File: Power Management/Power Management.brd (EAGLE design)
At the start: 22.2 x 10.2 mm, 7 parts, among them IC1 BH67172NUX, IC2 BH67172NUX, X1 52745-0690, X2 52745-0690

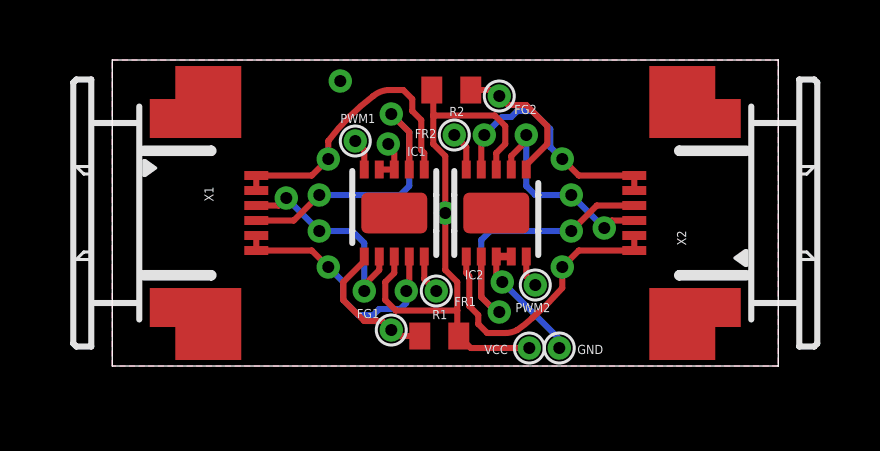
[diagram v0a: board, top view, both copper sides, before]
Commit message: Added Power Management reference design
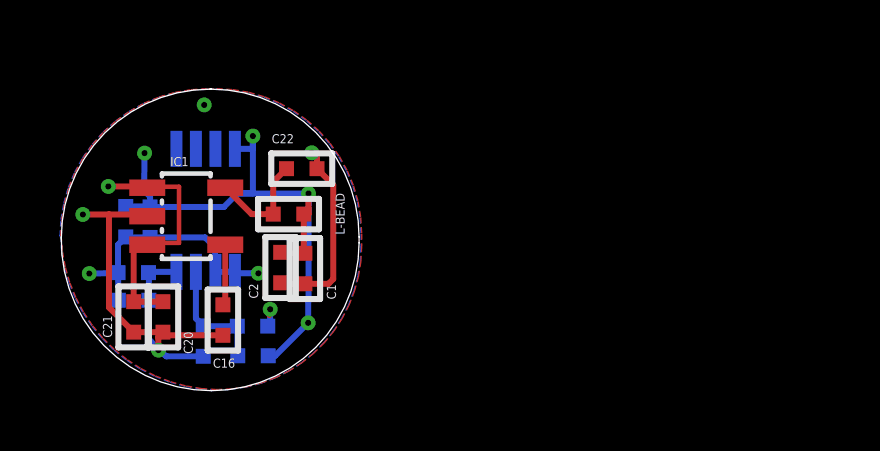
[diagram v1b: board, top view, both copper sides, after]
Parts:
- removed X1, X2: 52745-0690, con-molex:52745-0690
- added C1, C10, C11, C21: 10u, rc-master-smd:C0402
- added C16, C23: 10n, rc-master-smd:C0402
- added C2, C20, C22, C4, C5: 100n, rc-master-smd:C0402
- added L-BEAD: (no value), L-Bead:0402
- IC1: value BH67172NUX -> TPS732XX; device rohm:VSON010X3030 -> TPS732xx:SOT23
- IC2: value BH67172NUX -> AD8617; device rohm:VSON010X3030 -> ad8617:MSOP8
- R1, R2: value 10k -> (none); device resistor:R0402 -> rc-master-smd:R0402
- moved GOLD_ORB_SM1 16.0 mm to (12.6, 2.20)
- moved R2 10.3 mm to (7.28, 2.83), flipped to the bottom, turned to 0 degrees
- moved IC2 9.69 mm to (5.71, 6.69), flipped to the bottom, turned to 0 degrees
- moved IC1 6.94 mm to (5.07, 6.49), turned to 270 degrees
- moved R1 6.25 mm to (7.29, 1.84), flipped to the bottom, turned to 180 degrees
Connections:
- removed net +3V3: IC1.3, IC2.3, R1.2, R2.2
- removed net COM1: IC1.2, X1.3
- removed net COM2: IC2.2, X2.3
- removed net FG1: IC1.1, R1.1
- removed net FG2: IC2.1, R2.1
- removed net FR1: IC1.5
- removed net FR2: IC2.5
- removed net GND: IC1.8, IC1.9, IC2.8, IC2.9
- removed net PWM1: IC1.10
- removed net PWM2: IC2.10
- removed net U1: IC1.4, X1.5, X1.6
- removed net U2: IC2.4, X2.5, X2.6
- removed net V1: IC1.7, X1.4
- removed net V2: IC2.7, X2.4
- removed net W1: IC1.6, X1.1, X1.2
- removed net W2: IC2.6, X2.1, X2.2
- new net AGND: C10.2, C11.1, C4.2, C5.1, IC2.1, IC2.2
- new net DGND: C1.1, C10.1, C16.2, C2.1, C20.2, C21.1, C22.2, C23.2, C5.2, IC1.2, IC2.4, R2.1
- new net N$2: C23.1, IC2.3, R1.1, R2.2
- new net N$20: C16.1, IC1.4
- new net N$21: C22.1, IC1.5, L-BEAD.1
- new net V+: C1.2, C11.2, C2.2, C4.1, IC2.8, L-BEAD.2, R1.2
- new net VCC: C20.1, C21.2, IC1.1, IC1.3
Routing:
- net DGND: track 0.00 -> 22.5 mm, vias 0 -> 5
- net V+: track 0.00 -> 20.9 mm, vias 0 -> 4
- net +3V3: track 19.3 -> 0.00 mm, vias 2 -> 0
- net V2: track 10.4 -> 0.00 mm, vias 2 -> 0
- net V1: track 10.3 -> 0.00 mm, vias 2 -> 0
- net W1: track 9.83 -> 0.00 mm, vias 1 -> 0
- net W2: track 9.73 -> 0.00 mm, vias 1 -> 0
- net VCC: track 0.00 -> 8.75 mm, vias 0 -> 1
- net AGND: track 0.00 -> 8.60 mm, vias 0 -> 2
- net U1: track 8.50 -> 0.00 mm, vias 2 -> 0
- net U2: track 8.26 -> 0.00 mm, vias 2 -> 0
- net COM2: track 7.34 -> 0.00 mm, vias 3 -> 0
- net COM1: track 7.28 -> 0.00 mm, vias 3 -> 0
- net GND: track 5.85 -> 0.00 mm, vias 4 -> 0
- net FG2: track 4.79 -> 0.00 mm, vias 1 -> 0
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- added copper zone on layer 1, net DGND
- added copper zone on layer 16, net DGND
- removed copper zone on layer 1, net GND
- removed copper zone on layer 16, net GND
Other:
- board size 22.2 x 10.2 mm -> 9.9 x 10.1 mm
- board text removed: "BH67172NUX-FPC"
- board text removed: "FG1"
- board text removed: "FG2"
- board text removed: "FR1"
- board text removed: "FR2"
- board text removed: "GND"
- board text removed: "PWM1"
- board text removed: "PWM2"
- board text removed: "VCC"
